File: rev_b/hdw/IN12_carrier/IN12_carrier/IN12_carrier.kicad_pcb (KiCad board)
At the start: 4 copper layers, 200 x 50 mm, 189 parts, among them J1101 Power, J1102 Left, J1103 Right, J1104 Up, J1105 Down, J201 Conn_02x32_Top_Bottom, Q401 MMSTA42, Q402 MMSTA42, Q403 MMSTA42, Q404 MMSTA92, Q405 MMSTA92, Q406 MMSTA92, Q407 MMSTA42, Q408 MMSTA42, Q409 MMSTA42, Q410 MMSTA92, Q411 MMSTA92, Q412 MMSTA92, Q501 MMSTA42, Q502 MMSTA42, Q503 MMSTA42, Q504 MMSTA42, Q505 MMSTA42, Q506 MMSTA42, Q507 MMSTA42, Q508 MMSTA42, Q509 MMSTA42, Q510 MMSTA42, Q511 MMSTA42, Q512 MMSTA42, Q513 MMSTA42, Q514 MMSTA42, Q515 MMSTA42, U1001 TCA9555RGER, U1002 24AA02-OT, U1003 MAX6816, U1004 MAX6816, U1005 MAX6816, U1006 MAX6816, U1007 MAX6816, U301 DS1683, U302 LTC4316DD, U701 LP5009, U702 LP5009, U703 LP5009

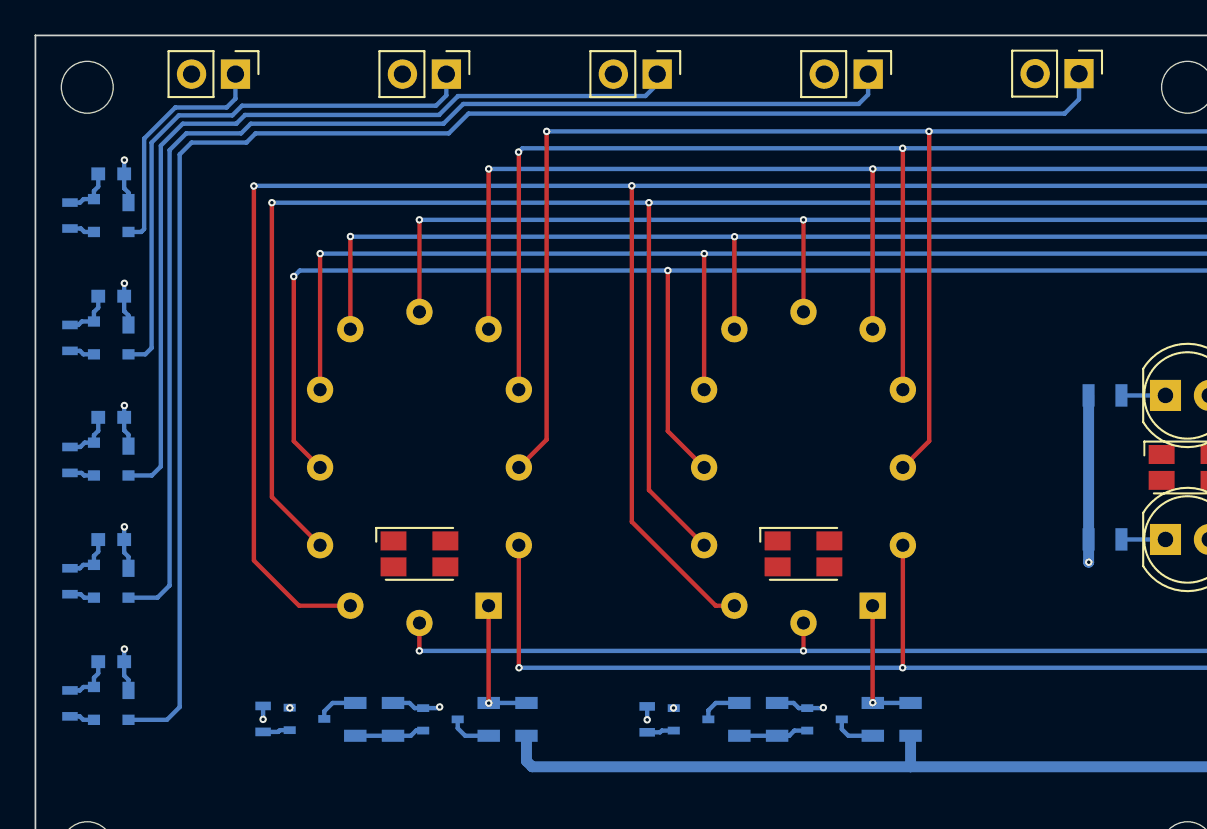
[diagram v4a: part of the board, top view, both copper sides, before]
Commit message: added cap touch sensors back
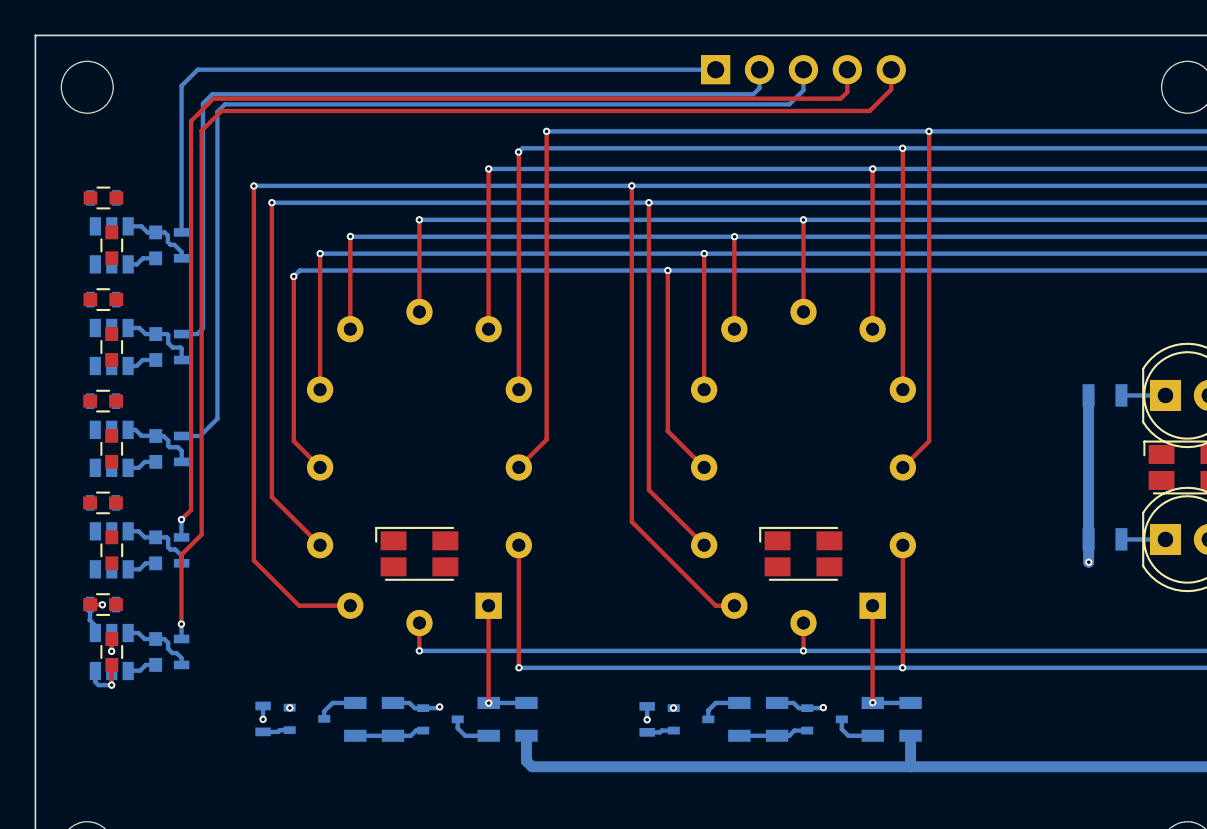
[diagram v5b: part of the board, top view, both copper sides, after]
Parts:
- removed J1101: Power, Connector_PinHeader_2.54mm:PinHeader_1x02_P2.54mm_Vertical
- removed J1102: Left, Connector_PinHeader_2.54mm:PinHeader_1x02_P2.54mm_Vertical
- removed J1103: Right, Connector_PinHeader_2.54mm:PinHeader_1x02_P2.54mm_Vertical
- removed J1104: Up, Connector_PinHeader_2.54mm:PinHeader_1x02_P2.54mm_Vertical
- removed J1105: Down, Connector_PinHeader_2.54mm:PinHeader_1x02_P2.54mm_Vertical
- added C1008: 10nF, Capacitors_SMD:C_0603, B.Cu at (42.2, 106.3)
- added C1009: 10nF, Capacitors_SMD:C_0603, B.Cu at (42.2, 112.1)
- added C1010: 10nF, Capacitors_SMD:C_0603, B.Cu at (42.2, 118.0)
- added C1011: 0.1uF, Capacitors_SMD:C_0603, F.Cu at (39.7, 100.4)
- added C1012: 0.1uF, Capacitors_SMD:C_0603, F.Cu at (39.7, 106.3)
- added C1013: 0.1uF, Capacitors_SMD:C_0603, F.Cu at (39.7, 112.1)
- added C1014: 0.1uF, Capacitors_SMD:C_0603, F.Cu at (39.7, 118.0)
- added C1015: 0.1uF, Capacitors_SMD:C_0603, F.Cu at (39.2, 97.6)
- added C1016: 10nF, Capacitors_SMD:C_0603, B.Cu at (42.2, 94.5)
- added C1017: 0.1uF, Capacitors_SMD:C_0603, F.Cu at (39.7, 94.5)
- added J1001: Cap SNS, Connector_PinHeader_2.54mm:PinHeader_1x05_P2.54mm_Horizontal, B.Cu at (74.6, 84.3)
- added R1017: 499, Resistors_SMD:R_0603, B.Cu at (43.7, 106.3)
- added R1018: 499, Resistors_SMD:R_0603, B.Cu at (43.7, 112.1)
- added R1019: 499, Resistors_SMD:R_0603, B.Cu at (43.7, 118.0)
- added R1020: 10k, Resistors_SMD:R_0603, B.Cu at (39.2, 97.6)
- added R1021: 499, Resistors_SMD:R_0603, B.Cu at (43.7, 94.5)
- C1003, C1004, C1005, C1006: moved to F.Cu
- C1007: value 0.1uF -> 10nF
- R1016: value 10k -> 499
- U1003, U1004, U1005, U1006, U1007: value MAX6816 -> AT42QT1010-TSHR; footprint Package_TO_SOT_SMD:SOT-143 -> TO_SOT_Packages_SMD:SOT-23-6
- moved R1015 29.3 mm to (39.2, 91.7), turned to 0 degrees
- moved C1006 26.8 mm to (39.2, 91.7)
- moved C1005 10.8 mm to (39.2, 115.3)
- moved C1007 10.3 mm to (42.2, 100.4), turned to 90 degrees
- moved R1016 9.98 mm to (43.7, 100.4)
- moved R1014 8.59 mm to (39.2, 115.3), turned to 0 degrees
- moved U1004 7.66 mm to (39.7, 106.3), turned to -90 degrees
- moved C1003 6.09 mm to (39.2, 103.5)
- moved U1005 5.28 mm to (39.7, 112.1), turned to -90 degrees
- moved R1013 4.92 mm to (39.2, 109.4), turned to 0 degrees
- moved R1012 4.13 mm to (39.2, 103.5), turned to 0 degrees
- moved U1006 2.98 mm to (39.7, 118.0), turned to -90 degrees
- moved C1004 2.17 mm to (39.2, 109.4)
- moved U1007 1.73 mm to (39.7, 94.5), turned to -90 degrees
- moved U1003 0.53 mm to (39.7, 100.4), turned to -90 degrees
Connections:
- C1003 pad 1: +3.3V -> Pushbutton_Right
- C1004 pad 1: +3.3V -> Pushbutton_Up
- C1005 pad 1: +3.3V -> Pushbutton_Down
- C1006 pad 1: +3.3V -> Pushbutton_Power
- C1007 pad 1: +3.3V -> Net-(U1003-SNS)
- C1007 pad 2: GND -> Net-(U1003-SNSK)
- R1012 pad 1: +3.3V -> Pushbutton_Right
- R1012 pad 2: Pushbutton_Left -> GND
- R1013 pad 1: +3.3V -> Pushbutton_Up
- R1013 pad 2: Pushbutton_Up -> GND
- R1014 pad 1: +3.3V -> Pushbutton_Down
- R1014 pad 2: Pushbutton_Right -> GND
- R1015 pad 1: +3.3V -> Pushbutton_Power
- R1015 pad 2: Pushbutton_Down -> GND
- R1016 pad 1: +3.3V -> Pushbutton_Left_SNS
- R1016 pad 2: Pushbutton_Power -> Net-(U1003-SNSK)
- U1003 pad 1: GND -> Pushbutton_Left
- U1003 pad 2: Net-(J1102-Pin_1) -> GND
- U1003 pad 3: Pushbutton_Left -> Net-(U1003-SNSK)
- U1003 pad 4: +3.3V -> Net-(U1003-SNS)
- U1004 pad 1: GND -> Pushbutton_Right
- U1004 pad 2: Net-(J1104-Pin_1) -> GND
- U1004 pad 3: Pushbutton_Up -> Net-(U1004-SNSK)
- U1004 pad 4: +3.3V -> Net-(U1004-SNS)
- U1005 pad 1: GND -> Pushbutton_Up
- U1005 pad 2: Net-(J1103-Pin_1) -> GND
- U1005 pad 3: Pushbutton_Right -> Net-(U1005-SNSK)
- U1005 pad 4: +3.3V -> Net-(U1005-SNS)
- U1006 pad 1: GND -> Pushbutton_Down
- U1006 pad 2: Net-(J1105-Pin_1) -> GND
- U1006 pad 3: Pushbutton_Down -> Net-(U1006-SNSK)
- U1006 pad 4: +3.3V -> Net-(U1006-SNS)
- U1007 pad 1: GND -> Pushbutton_Power
- U1007 pad 2: Net-(J1101-Pin_1) -> GND
- U1007 pad 3: Pushbutton_Power -> Net-(U1007-SNSK)
- U1007 pad 4: +3.3V -> Net-(U1007-SNS)
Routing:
- net Net-(J1105-Pin_1): track 90.1 -> 0.00 mm
- net Pushbutton_Down_SNS: track 0.00 -> 71.9 mm, vias 0 -> 1
- net Net-(J1104-Pin_1): track 70.8 -> 0.00 mm
- net Pushbutton_Up_SNS: track 0.00 -> 64.3 mm, vias 0 -> 1
- net Pushbutton_Right_SNS: track 0.00 -> 55.9 mm
- net Net-(J1103-Pin_1): track 51.4 -> 0.00 mm
- net Pushbutton_Left_SNS: track 0.00 -> 48.0 mm
- net Pushbutton_Power_SNS: track 0.00 -> 39.8 mm
- net Net-(J1102-Pin_1): track 32.8 -> 0.00 mm
- net Net-(J1101-Pin_1): track 13.9 -> 0.00 mm
- net +3.3V: track 22.8 -> 11.2 mm, vias 4 -> 5
- net GND: track 47.5 -> 36.7 mm, vias 46 -> 42
- net Net-(U1003-SNSK): track 0.00 -> 4.52 mm
- net Net-(U1004-SNSK): track 0.00 -> 4.42 mm
- net Net-(U1005-SNSK): track 0.00 -> 4.39 mm
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
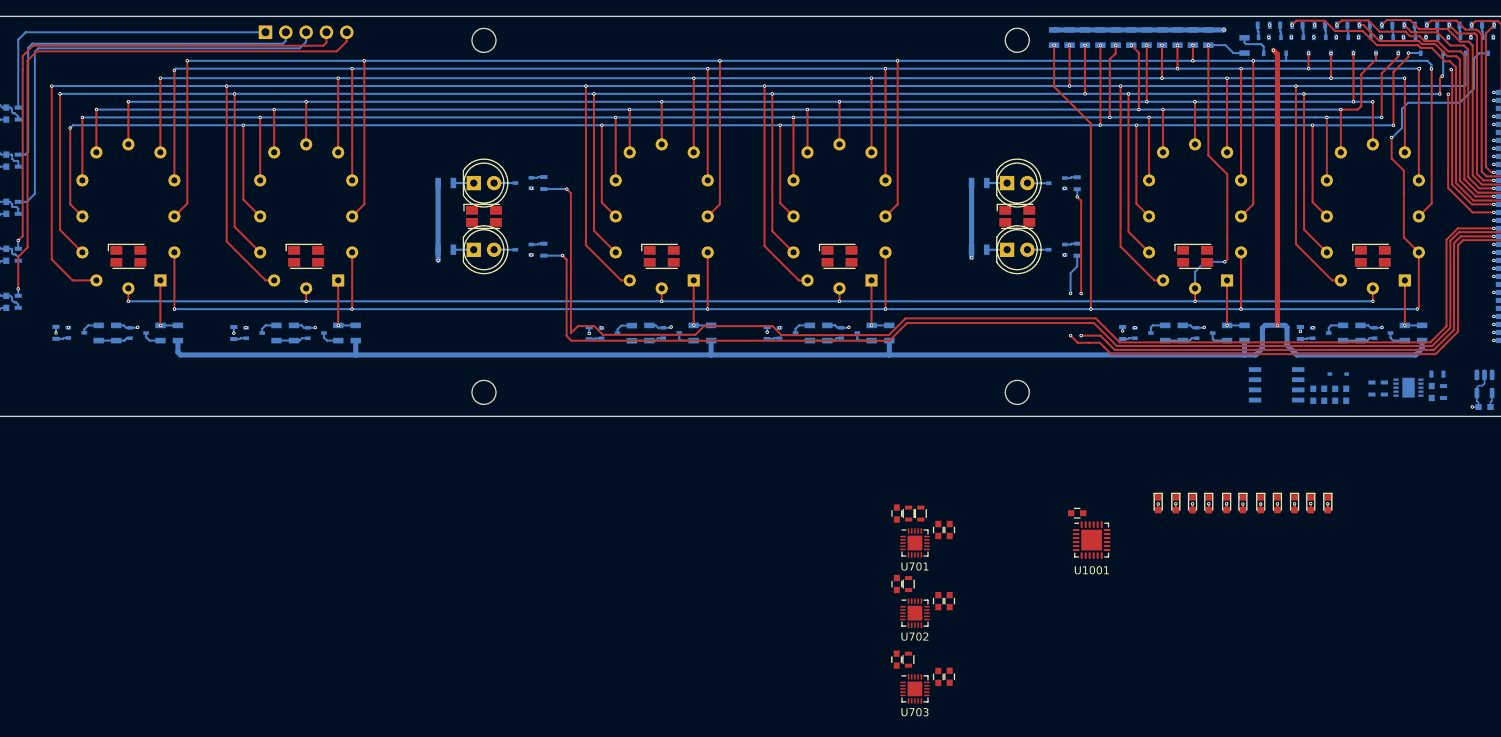
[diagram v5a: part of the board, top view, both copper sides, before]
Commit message: all components within IN12 carrier board outline
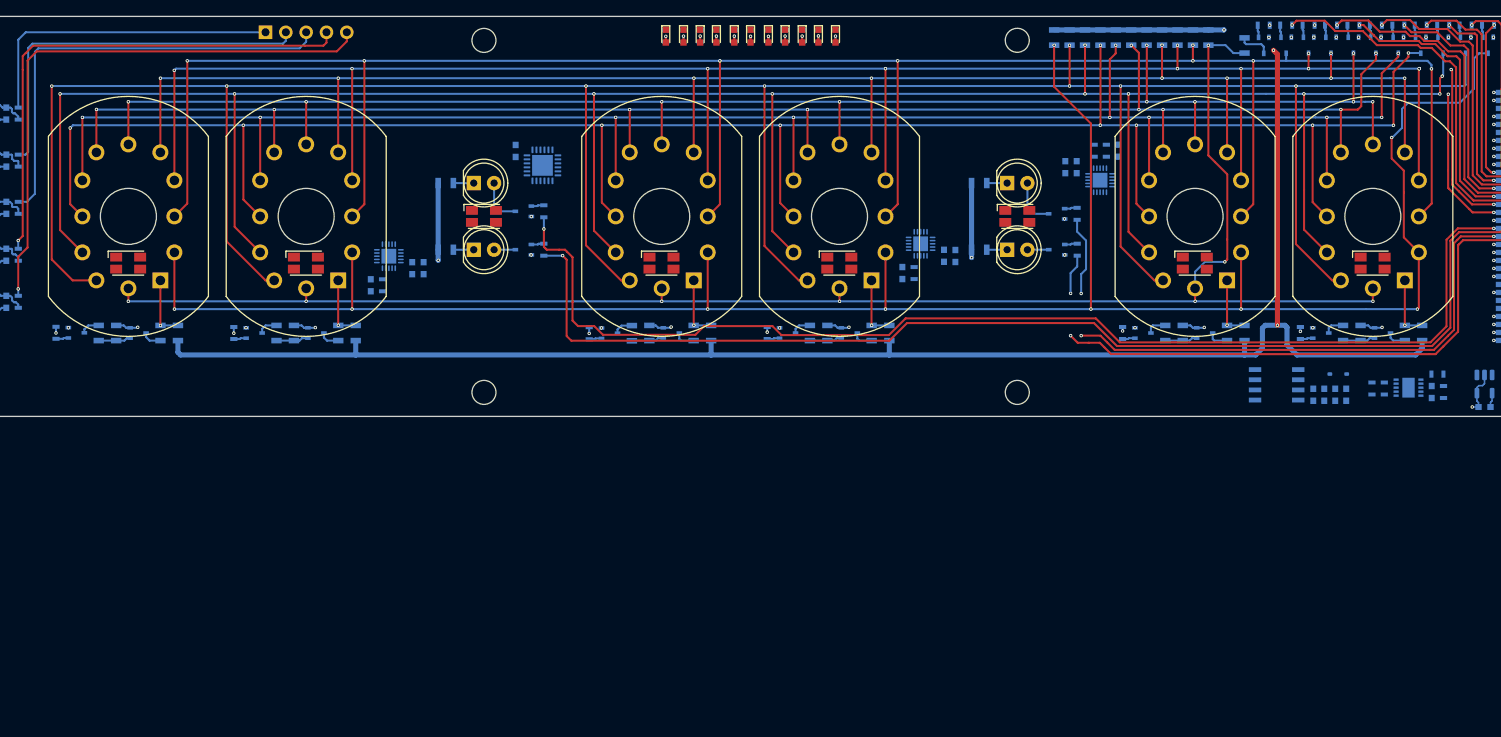
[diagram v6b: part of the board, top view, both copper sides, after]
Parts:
- C1002, C701, C702, C703, C704, C705, C706, C707, C708, C709, R701, R704, R705, R706, U1001, U701, U702, U703: moved to B.Cu
- moved D1001 84.9 mm to (124.7, 84.8)
- moved D1002 84.9 mm to (126.9, 84.8)
- moved D1003 84.9 mm to (129.0, 84.8)
- moved D1004 84.9 mm to (131.0, 84.8)
- moved D1005 84.9 mm to (133.2, 84.8)
- moved D1006 84.9 mm to (135.3, 84.8)
- moved D1007 84.9 mm to (137.5, 84.8)
- moved D1009 84.9 mm to (141.7, 84.8)
- moved D1010 84.9 mm to (143.7, 84.8)
- moved D1011 84.9 mm to (145.9, 84.8)
- moved R1001 84.9 mm to (124.7, 84.8)
- moved R1002 84.9 mm to (126.9, 84.8)
- moved R1003 84.9 mm to (129.0, 84.8)
- moved R1004 84.9 mm to (131.0, 84.8)
- moved R1005 84.9 mm to (133.2, 84.8)
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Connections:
- U1001 pad 1: Set_Brightness_LED -> Display_Time_LED
- U1001 pad 10: Display_Date_LED -> Alarm_Enable_LED
- U1001 pad 11: Set_Time_LED -> 24HR_Mode_LED
- U1001 pad 12: Display_Time_LED -> Set_Brightness_LED
- U1001 pad 2: 24HR_Mode_LED -> Set_Time_LED
- U1001 pad 3: Alarm_Enable_LED -> Display_Date_LED
- U1001 pad 4: Set_Alarm_LED -> Set_Date_LED
- U1001 pad 5: Display_Alarm_LED -> Display_Weekday_LED
- U1001 pad 7: Display_Weekday_LED -> Display_Alarm_LED
- U1001 pad 8: Set_Date_LED -> Set_Alarm_LED
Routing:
- net Colon_0_DSP: track 154.0 -> 148.3 mm
- net Colon_2_Cathode: track 2.68 -> 5.99 mm
- net Colon_2_DSP: track 84.5 -> 81.2 mm, vias 4 -> 3
- net Colon_0_Cathode: track 2.66 -> 5.80 mm
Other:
- board text added: "To-Do: * Fix net classing on misc HV nets to get correct clearance * Stackup legend * Stackup table * Owl * Board name * Board date * Board stats"
- board text removed: "To-Do: * Double check LED clearance from IN-12 hole * Check to see if IN12 footprint needs a hole * Double check IN12 pinout * Double check IN12 PTH drill size * Stackup legend * Stackup table * Owl * Board name * Board date * Board stats"

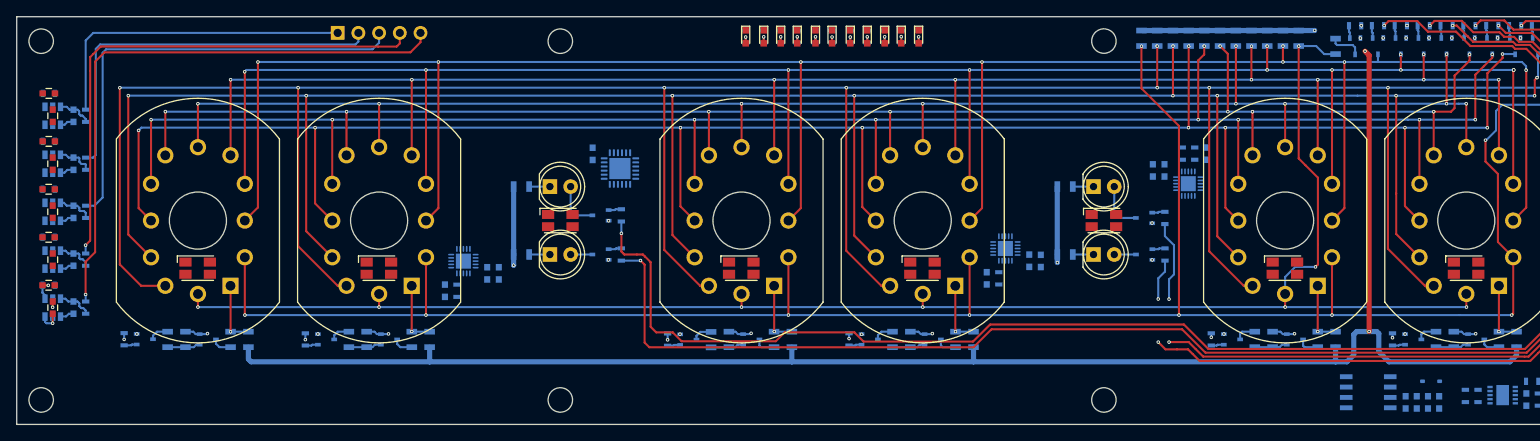
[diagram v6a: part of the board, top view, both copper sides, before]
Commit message: some misc signal routing on IN12 carrier
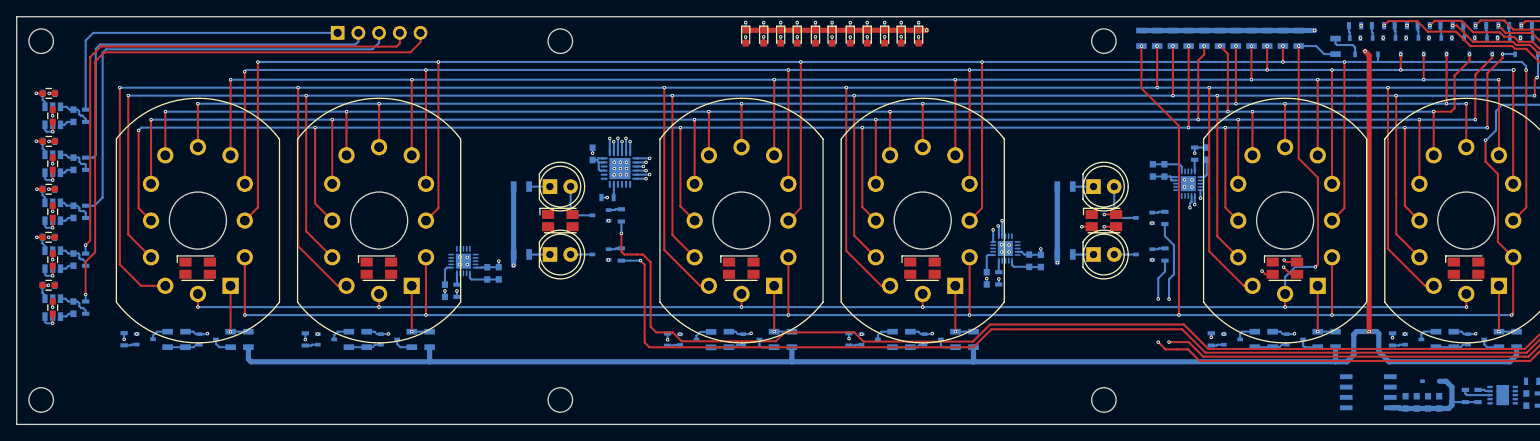
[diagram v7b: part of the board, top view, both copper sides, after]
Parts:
- moved R701 70.7 mm to (107.7, 104.5), turned to 180 degrees
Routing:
- net GND: track 36.7 -> 90.6 mm, vias 42 -> 82
- net Set_Brightness_LED: track 0.00 -> 51.7 mm, vias 0 -> 2
- net 24HR_Mode_LED: track 0.00 -> 47.5 mm, vias 0 -> 2
- net Display_Alarm_LED: track 0.00 -> 45.7 mm, vias 0 -> 2
- net Alarm_Enable_LED: track 0.00 -> 45.1 mm, vias 0 -> 2
- net Set_Alarm_LED: track 0.00 -> 42.1 mm, vias 0 -> 2
- net Set_Weekday_LED: track 0.00 -> 40.9 mm, vias 0 -> 2
- net Display_Weekday_LED: track 0.00 -> 39.7 mm, vias 0 -> 2
- net Set_Date_LED: track 0.00 -> 37.9 mm, vias 0 -> 2
- net Display_Date_LED: track 0.00 -> 35.0 mm, vias 0 -> 2
- net Set_Time_LED: track 0.00 -> 33.5 mm, vias 0 -> 2
- net +3.3V: track 11.2 -> 43.2 mm, vias 5 -> 9
- net Display_Time_LED: track 0.00 -> 31.8 mm, vias 0 -> 2
- net TUBE1_LED_G: track 0.00 -> 26.6 mm, vias 0 -> 2
- net TUBE1_LED_B: track 0.00 -> 22.4 mm, vias 0 -> 2
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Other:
- board text added: "To-Do: * Enter stackup in design rules * Stackup legend * Owl * Board name * Board date * Board stats"
- board text removed: "To-Do: * Fix net classing on misc HV nets to get correct clearance * Stackup legend * Stackup table * Owl * Board name * Board date * Board stats"
